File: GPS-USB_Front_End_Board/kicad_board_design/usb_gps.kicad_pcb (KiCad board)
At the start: 4 copper layers, 99.1 x 53.3 mm, 291 parts, among them J1 Micro-USB Connector, J3 SMA, P1 CONN_02X12, P2 CONN_01X03, U1 93LCxxB, U2 FT2232HL-REEL, U3 L4931 LDO, U4 MAX8510, U5 MAX8510, U6 MAX2771, U7 SAWTEK-855969, U8 LT1719S6 -- Not Populated, X1 13.368MHz TCXO, Y1 12MHz Crystal

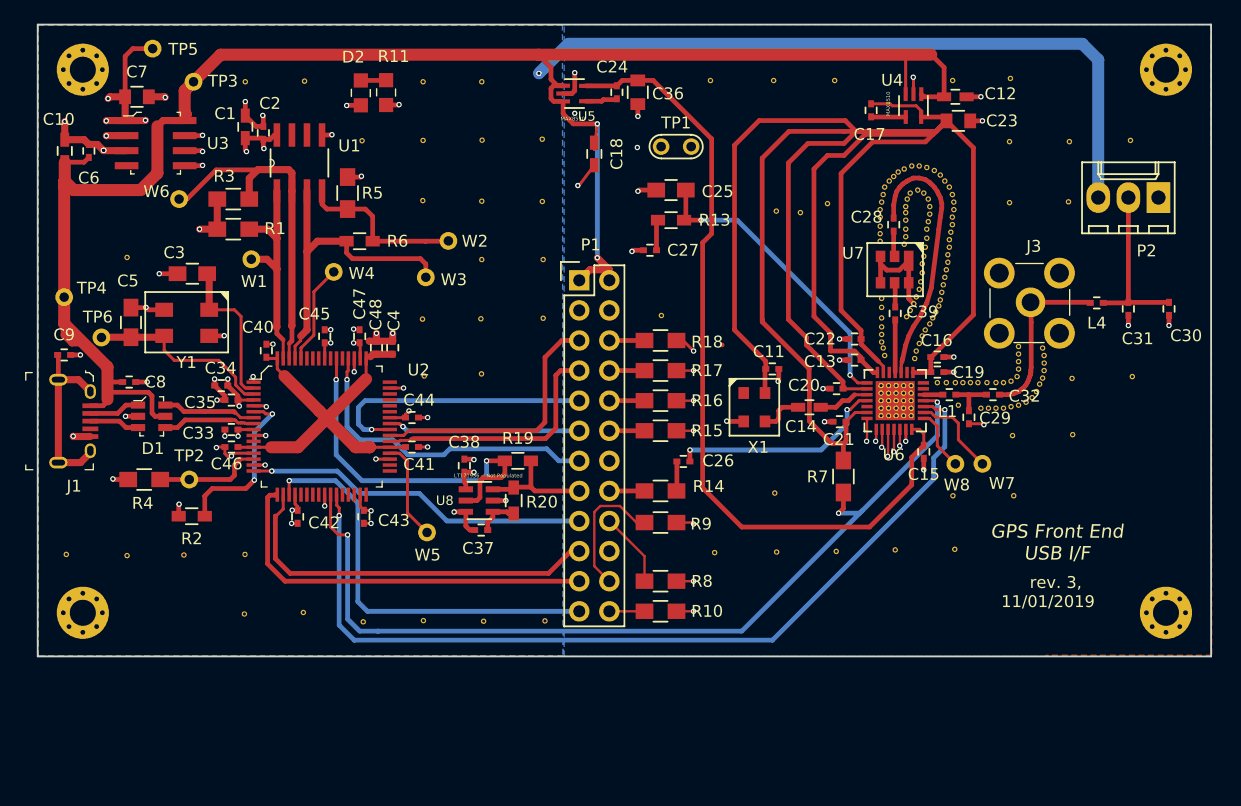
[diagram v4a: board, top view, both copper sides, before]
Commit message: Add signals to header.
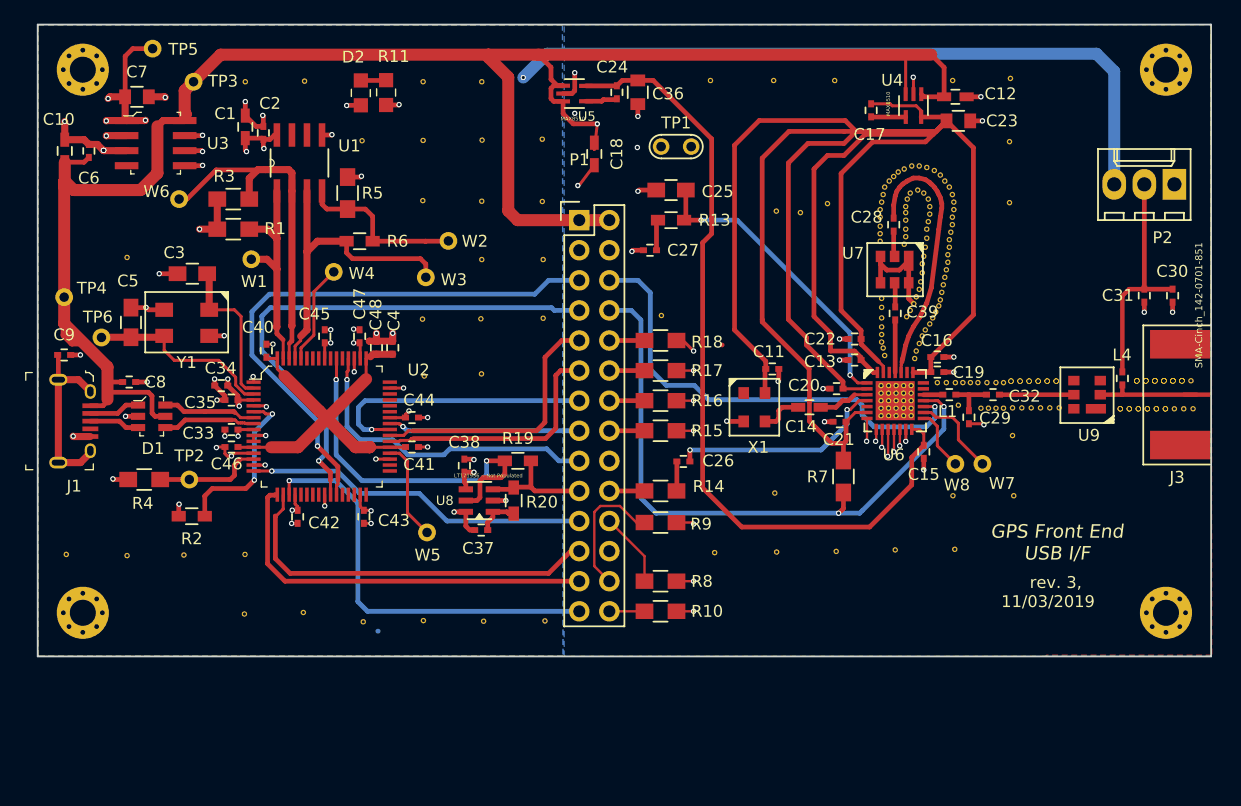
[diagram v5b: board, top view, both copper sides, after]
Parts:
- removed the REF** at (174.8, 70.7)
- removed the REF** at (167.4, 88.3)
- removed the REF** at (165.2, 90.7)
- removed the REF** at (165.4, 90.0)
- removed the REF** at (165.4, 89.4)
- removed the REF** at (165.4, 88.8)
- removed the REF** at (165.4, 88.1)
- removed the REF** at (175.0, 90.7)
- removed the REF** at (169.9, 90.8)
- removed the REF** at (169.9, 95.6)
- removed the REF** at (169.6, 70.8)
- removed the REF** at (169.6, 75.9)
- removed the REF** at (165.4, 93.1)
- removed the REF** at (166.0, 92.8)
- removed the REF** at (166.5, 92.5)
- removed the REF** at (166.9, 91.9)
- removed the REF** at (167.1, 91.3)
- removed the REF** at (167.4, 90.8)
- removed the REF** at (167.5, 90.2)
- removed the REF** at (167.5, 89.5)
- removed the REF** at (167.5, 88.9)
- added REF**: via_10mil, logo:via_10mil, F.Cu at (179.9, 91.0)
- added REF** (x2): via_10mil, logo:via_10mil, F.Cu at (177.7, 93.4)
- added REF** (x2): via_10mil, logo:via_10mil, F.Cu at (177.0, 93.4)
- added REF** (x2): via_10mil, logo:via_10mil, F.Cu at (176.2, 93.4)
- added REF** (x2): via_10mil, logo:via_10mil, F.Cu at (175.5, 93.4)
- added REF** (x2): via_10mil, logo:via_10mil, F.Cu at (174.7, 93.4)
- added REF** (x2): via_10mil, logo:via_10mil, F.Cu at (173.9, 93.4)
- added REF**: via_10mil, logo:via_10mil, F.Cu at (164.7, 91.1)
- added REF** (x2): via_10mil, logo:via_10mil, F.Cu at (165.5, 91.1)
- added REF** (x2): via_10mil, logo:via_10mil, F.Cu at (166.2, 91.1)
- added REF**: via_10mil, logo:via_10mil, F.Cu at (178.5, 93.4)
- added REF** (x2): via_10mil, logo:via_10mil, F.Cu at (167.0, 91.1)
- added REF** (x2): via_10mil, logo:via_10mil, F.Cu at (167.8, 91.1)
- added REF** (x2): via_10mil, logo:via_10mil, F.Cu at (168.5, 91.1)
- added REF** (x4): via_10mil, logo:via_10mil, F.Cu at (179.1, 91.0)
- added REF** (x4): via_10mil, logo:via_10mil, F.Cu at (178.4, 91.0)
- added REF** (x4): via_10mil, logo:via_10mil, F.Cu at (177.6, 91.0)
- added REF** (x4): via_10mil, logo:via_10mil, F.Cu at (176.9, 91.0)
- added REF** (x4): via_10mil, logo:via_10mil, F.Cu at (176.1, 91.0)
- added REF** (x4): via_10mil, logo:via_10mil, F.Cu at (175.3, 91.0)
- added REF**: via_10mil, logo:via_10mil, F.Cu at (179.3, 93.4)
- added REF**: via_10mil, logo:via_10mil, F.Cu at (180.1, 93.4)
- added REF**: via_10mil, logo:via_10mil, F.Cu at (168.8, 93.3)
- added REF**: via_10mil, logo:via_10mil, F.Cu at (168.0, 93.3)
- added REF**: via_10mil, logo:via_10mil, F.Cu at (167.2, 93.3)
- added REF**: via_10mil, logo:via_10mil, F.Cu at (166.4, 93.3)
- added REF**: via_10mil, logo:via_10mil, F.Cu at (165.6, 93.3)
- added U9: SAWTEK-855969, rf:Sawtek_855969, F.Cu at (171.9, 93.4)
- J3: value SMA -> SMA-Cinch_142-0701-851; footprint digikey-footprints:RF_SMA_Vertical_5-1814832-1 -> rf:Cinch_142-0701-851
- P1: value CONN_02X12 -> CONN_02X14; footprint Pin_Headers:Pin_Header_Straight_2x12 -> Pin_Headers:Pin_Header_Straight_2x14
- U8: footprint rf:TSOT-23_S6 -> TSOT-23_S6
- moved J3 17.1 mm to (181.5, 92.2), turned to 270 degrees
- moved L4 6.73 mm to (174.1, 90.8), turned to 270 degrees
- moved P1 5.08 mm to (128.3, 77.5)
- moved C31 1.75 mm to (176.0, 83.8)
- moved P2 1.75 mm to (178.5, 74.4)
- moved C30 1.16 mm to (178.4, 83.8)
- moved REF** 0.16 mm to (164.8, 93.3)
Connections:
- net /MAX_2769/MIXIN renamed Net-(C39-Pad2)
- J3 pad 2: Net-(C32-Pad1) -> Net-(J3-Pad2)
- L4 pad 2: Net-(C32-Pad1) -> Net-(J3-Pad2)
- P1 pad 10: /MAX_2769/D2 -> /MAX_2769/D0
- P1 pad 11: /USB_FT2232/D3 -> /USB_FT2232/D0
- P1 pad 12: /MAX_2769/D3 -> /MAX_2769/D1
- P1 pad 13: /USB_FT2232/TXE# -> /USB_FT2232/D2
- P1 pad 14: Net-(P1-Pad14) -> /MAX_2769/D2
- P1 pad 15: /USB_FT2232/WR# -> /USB_FT2232/D3
- P1 pad 16: /MAX_2769/WR# -> /MAX_2769/D3
- P1 pad 17: /USB_FT2232/SCLK -> /USB_FT2232/TXE#
- P1 pad 18: /MAX_2769/SCLK -> Net-(P1-Pad18)
- P1 pad 19: /USB_FT2232/SDI -> /USB_FT2232/WR#
- P1 pad 20: Net-(P1-Pad20) -> /MAX_2769/WR#
- P1 pad 21: /USB_FT2232/SDO -> /USB_FT2232/SCLK
- P1 pad 22: /MAX_2769/SDO -> /MAX_2769/SCLK
- P1 pad 23: /USB_FT2232/SCS -> /USB_FT2232/SDI
- P1 pad 24: /MAX_2769/SCS -> Net-(P1-Pad24)
- P1 pad 5: /USB_FT2232/D1 -> /USB_FT2232/GPIO1
- P1 pad 6: /MAX_2769/D0 -> /MAX_2769/LD
- P1 pad 7: /USB_FT2232/D0 -> /USB_FT2232/GPIO0
- P1 pad 8: /MAX_2769/D1 -> /MAX_2769/SHDN#
- P1 pad 9: /USB_FT2232/D2 -> /USB_FT2232/D1
- R7 pad 1: /USB_FT2232/GPIO0 -> /MAX_2769/SHDN#
- U6 pad 17: /USB_FT2232/GPIO1 -> /MAX_2769/LD
- U6 pad 18: /USB_FT2232/GPIO0 -> /MAX_2769/SHDN#
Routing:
- net /MAX_2769/SHDN#: track 0.00 -> 52.8 mm, vias 0 -> 2
- net /MAX_2769/LD: track 0.00 -> 39.1 mm, vias 0 -> 1
- net /USB_FT2232/GPIO0: track 76.7 -> 45.2 mm, vias 3 -> 1
- net /USB_FT2232/GPIO1: track 75.6 -> 47.3 mm, vias 2 -> 1
- net Net-(J3-Pad2): track 0.00 -> 9.01 mm
- net /MAX_2769/+5V: track 187.2 -> 178.3 mm, vias 2 -> 1
- net Net-(C32-Pad1): track 14.6 -> 6.28 mm
- net Net-(C30-Pad1): track 14.4 -> 19.8 mm
- net GND: track 98.3 -> 96.6 mm
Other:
- board text added: "rev. 3, 11/03/2019"
- board text removed: "rev. 3, 11/01/2019"
